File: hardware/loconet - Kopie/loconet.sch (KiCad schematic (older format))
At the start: 40 parts, among them J1 RJ12, J10 PWR, J11 PullUpEnable, J2 RJ12, J3 DCC, J4 Arduino Sockelleiste Pin01-15, J5 Arduino Sockelleiste Pin16-30, J6 PCA9685, J7 SCL/SDA, J8 I²C Connector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

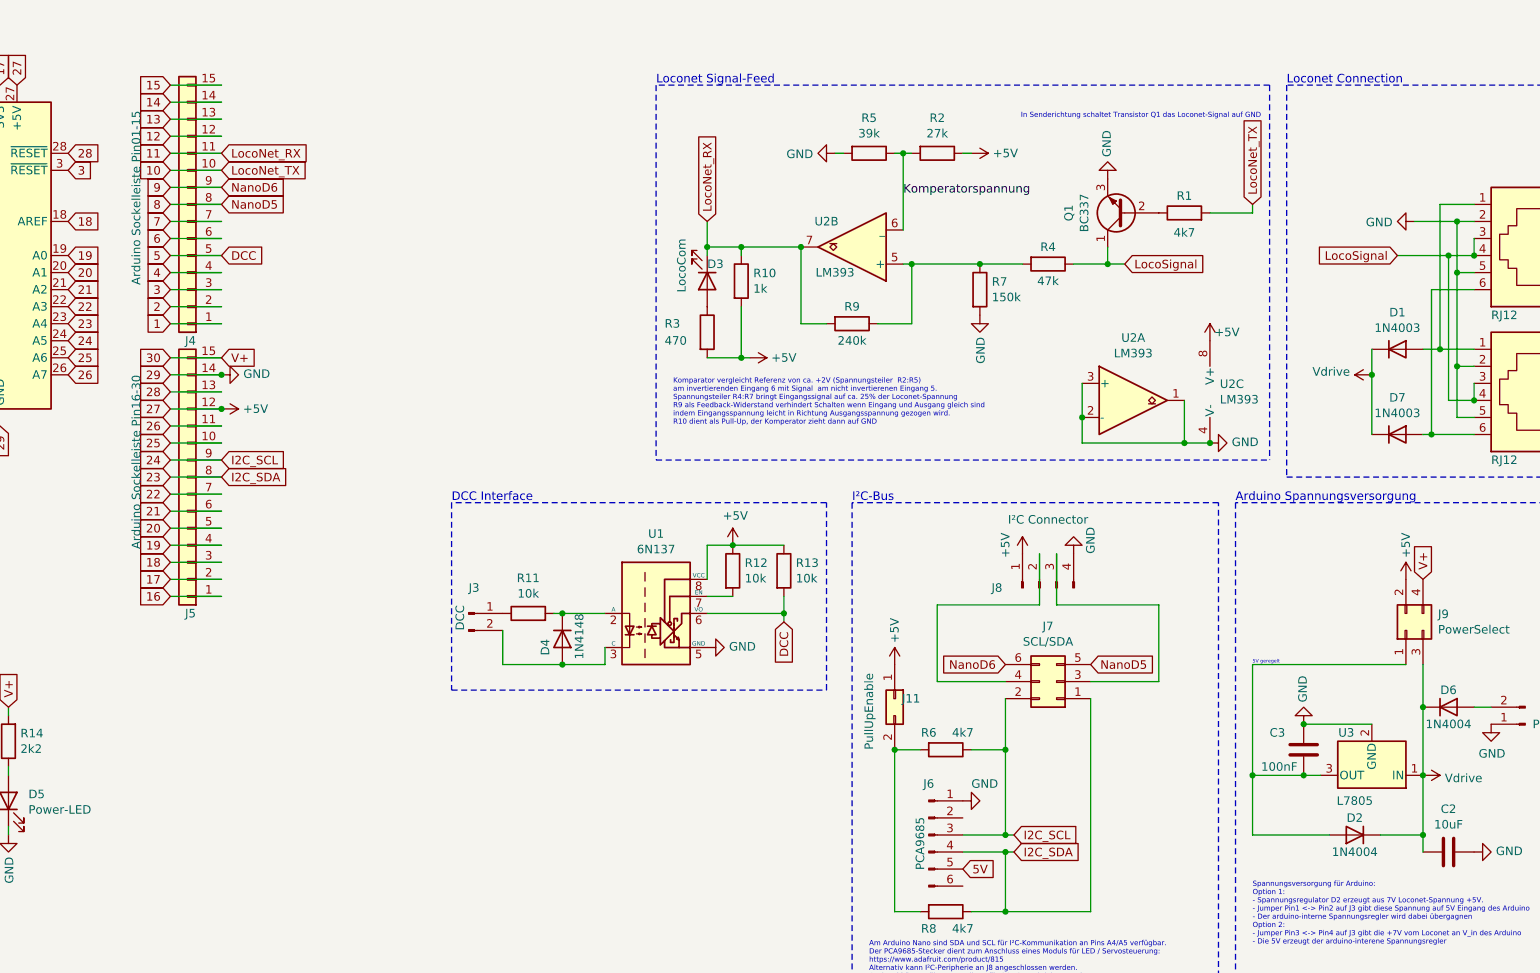
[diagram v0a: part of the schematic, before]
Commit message: Add variant hardware with loconet TX indicator LED
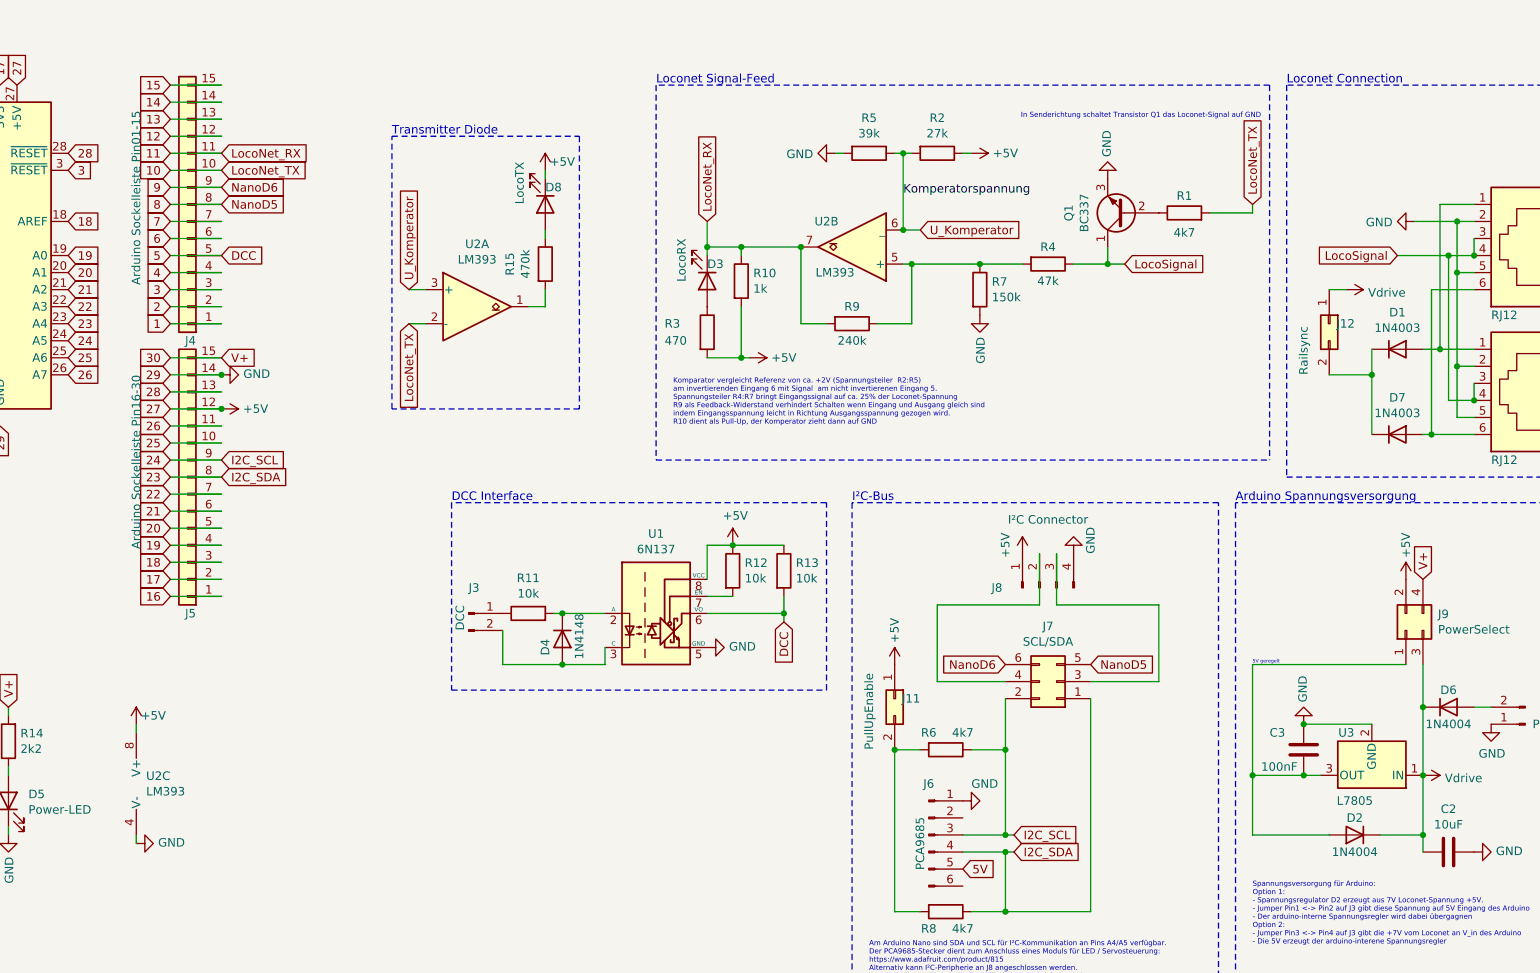
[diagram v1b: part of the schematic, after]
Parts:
- added D8: LocoTX, LED_THT:LED_D3.0mm, symbol Device:LED
- added J12: Railsync, Connector_PinHeader_2.54mm:PinHeader_2x01_P2.54mm_Vertical, symbol Connector_Generic:Conn_02x01
- added R15: 470k, Resistor_THT:R_Axial_DIN0207_L6.3mm_D2.5mm_P7.62mm_Horizontal, symbol Device:R
- D3: value LocoCom -> LocoRX
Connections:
- net +5V: now also D8.1 (K)
- net 10: now also U2.2 (-)
- net GND: no longer U2.1, U2.2 (-), U2.3 (+)
- net Vdrive: now also J12.1 (Pin_1); no longer D1.1 (K), D7.1 (K)
- net Komperatorspannung renamed U_Komperator
- net U_Komperator: now also U2.3 (+)
- new net: D1.1 (K), D7.1 (K), J12.2 (Pin_2)
- new net: R15.2, U2.1
- new net: D8.2 (A), R15.1
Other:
- note added: "Transmitter Diode"
- moved on the sheet: U2A, U2C
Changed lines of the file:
@@
 	1    0    0    -1
 $EndComp
-$Comp
-L Device:LED D3
-U 1 1 5EB93691
-P 5650 1850
-F 0 "D3" V 5550 1850 50  0000 L CNN
-F 1 "LocoCom" H 5400 1700 50  0000 L CNN
-F 2 "LED_THT:LED_D3.0mm" H 5650 1850 50  0001 C CNN
-F 3 "~" H 5650 1850 50  0001 C CNN
-	1    5650 1850
-	0    1    1    0
-$EndComp
 Wire Wire Line
 	10150 1400 9950 1400
@@
 	9900 1900 10150 1900
 Wire Wire Line
-	9550 2250 9550 2400
-Wire Wire Line
 	10150 1600 10150 1700
 Connection ~ 10150 1700
@@
 L Comparator:LM393 U2
 U 1 1 5EDB1EB7
-P 8150 2550
-F 0 "U2" H 8150 2917 50  0000 C CNN
-F 1 "LM393" H 8150 2826 50  0000 C CNN
-F 2 "" H 8150 2550 50  0001 C CNN
-F 3 "http://www.ti.com/lit/ds/symlink/lm393-n.pdf" H 8150 2550 50  0001 C CNN
-	1    8150 2550
+P 4300 2000
+F 0 "U2" H 4300 2367 50  0000 C CNN
+F 1 "LM393" H 4300 2276 50  0000 C CNN
+F 2 "" H 4300 2000 50  0001 C CNN
+F 3 "http://www.ti.com/lit/ds/symlink/lm393-n.pdf" H 4300 2000 50  0001 C CNN
+	1    4300 2000
 	1    0    0    -1
 $EndComp
@@
 L Comparator:LM393 U2
 U 3 1 5EDB30C8
-P 8700 2500
-F 0 "U2" H 8658 2546 50  0000 L CNN
-F 1 "LM393" H 8658 2455 50  0000 L CNN
-F 2 "" H 8700 2500 50  0001 C CNN
-F 3 "http://www.ti.com/lit/ds/symlink/lm393-n.pdf" H 8700 2500 50  0001 C CNN
-	3    8700 2500
+P 2400 4800
+F 0 "U2" H 2358 4846 50  0000 L CNN
+F 1 "LM393" H 2358 4755 50  0000 L CNN
+F 2 "" H 2400 4800 50  0001 C CNN
+F 3 "http://www.ti.com/lit/ds/symlink/lm393-n.pdf" H 2400 4800 50  0001 C CNN
+	3    2400 4800
 	1    0    0    -1
 $EndComp
@@
 L power:GND #PWR0101
 U 1 1 5EDB506B
-P 8600 2800
-F 0 "#PWR0101" H 8600 2550 50  0001 C CNN
-F 1 "GND" V 8605 2672 50  0000 R CNN
-F 2 "" H 8600 2800 50  0001 C CNN
-F 3 "" H 8600 2800 50  0001 C CNN
-	1    8600 2800
+P 2300 5150
+F 0 "#PWR0101" H 2300 4900 50  0001 C CNN
+F 1 "GND" V 2305 5022 50  0000 R CNN
+F 2 "" H 2300 5150 50  0001 C CNN
+F 3 "" H 2300 5150 50  0001 C CNN
+	1    2300 5150
 	0    -1   -1   0
 $EndComp
-Wire Wire Line
-	8600 2800 8450 2800
-Wire Wire Line
-	7850 2800 7850 2650
-Connection ~ 8600 2800
-Wire Wire Line
-	7850 2650 7850 2450
-Connection ~ 7850 2650
 $Comp
 L power:+5V #PWR0102
 U 1 1 5EDD0583
-P 8600 2200
-F 0 "#PWR0102" H 8600 2050 50  0001 C CNN
-F 1 "+5V" H 8700 2250 50  0000 C CNN
-F 2 "" H 8600 2200 50  0001 C CNN
-F 3 "" H 8600 2200 50  0001 C CNN
-	1    8600 2200
+P 2300 4450
+F 0 "#PWR0102" H 2300 4300 50  0001 C CNN
+F 1 "+5V" H 2400 4500 50  0000 C CNN
+F 2 "" H 2300 4450 50  0001 C CNN
+F 3 "" H 2300 4450 50  0001 C CNN
+	1    2300 4450
 	1    0    0    -1
 $EndComp
@@
 Entry Bus Bus
 	14700 -1150 14800 -1050
-Wire Wire Line
-	8450 2550 8450 2800
-Connection ~ 8450 2800
-Wire Wire Line
-	8450 2800 7850 2800
 $Comp
 L power:Vdrive #PWR07
 U 1 1 5F9BCDAB
-P 9550 2400
-F 0 "#PWR07" H 9350 2250 50  0001 C CNN
-F 1 "Vdrive" V 9568 2528 50  0000 L CNN
-F 2 "" H 9550 2400 50  0001 C CNN
-F 3 "" H 9550 2400 50  0001 C CNN
-	1    9550 2400
-	0    -1   -1   0
+P 9400 1900
+F 0 "#PWR07" H 9200 1750 50  0001 C CNN
+F 1 "Vdrive" V 9418 2028 50  0000 L CNN
+F 2 "" H 9400 1900 50  0001 C CNN
+F 3 "" H 9400 1900 50  0001 C CNN
+	1    9400 1900
+	0    1    1    0
 $EndComp
 $Comp
@@
 	0    1    1    0
 $EndComp
+Text Label 6800 1350 0    50   ~ 0
+Komperatorspannung
+Text GLabel 6900 1550 2    50   Input ~ 0
+U_Komperator
+Wire Wire Line
+	6800 1550 6900 1550
+Connection ~ 6800 1550
+$Comp
+L Device:R R15
+U 1 1 5FA24740
+P 4700 1750
+F 0 "R15" V 4493 1750 50  0000 C CNN
+F 1 "470k" V 4584 1750 50  0000 C CNN
+F 2 "Resistor_THT:R_Axial_DIN0207_L6.3mm_D2.5mm_P7.62mm_Horizontal" V 4630 1750 50  0001 C CNN
+F 3 "~" H 4700 1750 50  0001 C CNN
+	1    4700 1750
+	1    0    0    -1
+$EndComp
+Wire Wire Line
+	2300 4450 2300 4500
+Wire Wire Line
+	2300 5100 2300 5150
+$Comp
+L Device:LED D8
+U 1 1 5FA41AAA
+P 4700 1400
+F 0 "D8" V 4600 1400 50  0000 L CNN
+F 1 "LocoTX" H 4450 1250 50  0000 L CNN
+F 2 "LED_THT:LED_D3.0mm" H 4700 1400 50  0001 C CNN
+F 3 "~" H 4700 1400 50  0001 C CNN
+	1    4700 1400
+	0    1    1    0
+$EndComp
+Wire Wire Line
+	4700 1550 4700 1600
+Wire Wire Line
+	4700 1900 4700 2000
+Wire Wire Line
+	4700 1250 4700 1200
+Text GLabel 3900 1900 1    50   Input ~ 0
+U_Komperator
+Wire Wire Line
+	3900 1900 4000 1900
+Text GLabel 3900 2100 3    50   Input ~ 0
+LocoNet_TX
+Wire Wire Line
+	3900 2100 4000 2100
+Wire Wire Line
+	4600 2000 4700 2000
+$Comp
+L power:+5V #PWR0107
+U 1 1 5FA7987F
+P 4700 1200
+F 0 "#PWR0107" H 4700 1050 50  0001 C CNN
+F 1 "+5V" H 4800 1250 50  0000 C CNN
+F 2 "" H 4700 1200 50  0001 C CNN
+F 3 "" H 4700 1200 50  0001 C CNN
+	1    4700 1200
+	1    0    0    -1
+$EndComp
+Wire Notes Line
+	3800 1000 4900 1000
+Wire Notes Line
+	4900 1000 4900 2600
+Wire Notes Line
+	4900 2600 3800 2600
+Wire Notes Line
+	3800 2600 3800 1000
+Text Notes 3800 1000 0    50   ~ 0
+Transmitter Diode
+$Comp
+L Device:LED D3
+U 1 1 5EB93691
+P 5650 1850
+F 0 "D3" V 5550 1850 50  0000 L CNN
+F 1 "LocoRX" H 5400 1700 50  0000 L CNN
+F 2 "LED_THT:LED_D3.0mm" H 5650 1850 50  0001 C CNN
+F 3 "~" H 5650 1850 50  0001 C CNN
+	1    5650 1850
+	0    1    1    0
+$EndComp
+$Comp
+L Connector_Generic:Conn_02x01 J12
+U 1 1 5FB03C5E
+P 9300 2100
+F 0 "J12" V 9300 2250 50  0000 R CNN
+F 1 "Railsync" H 9600 1950 50  0000 R CNN
+F 2 "Connector_PinHeader_2.54mm:PinHeader_2x01_P2.54mm_Vertical" H 9300 2100 50  0001 C CNN
+F 3 "~" H 9300 2100 50  0001 C CNN
+	1    9300 2100
+	0    1    1    0
+$EndComp
+Wire Wire Line
+	9300 1900 9400 1900
+Wire Wire Line
+	9550 2250 9550 2400
+Wire Wire Line
+	9300 2400 9550 2400
 Connection ~ 9550 2400
 Wire Wire Line
 	9550 2400 9550 2750
-Text Label 6800 1350 0    50   ~ 0
-Komperatorspannung
 $EndSCHEMATC

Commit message: Einige Verbesserungen am PCB Layout
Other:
- moved on the sheet: C2, C3, D2, D4, D6, J10, J11, J3, J6, J7, J8, J9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

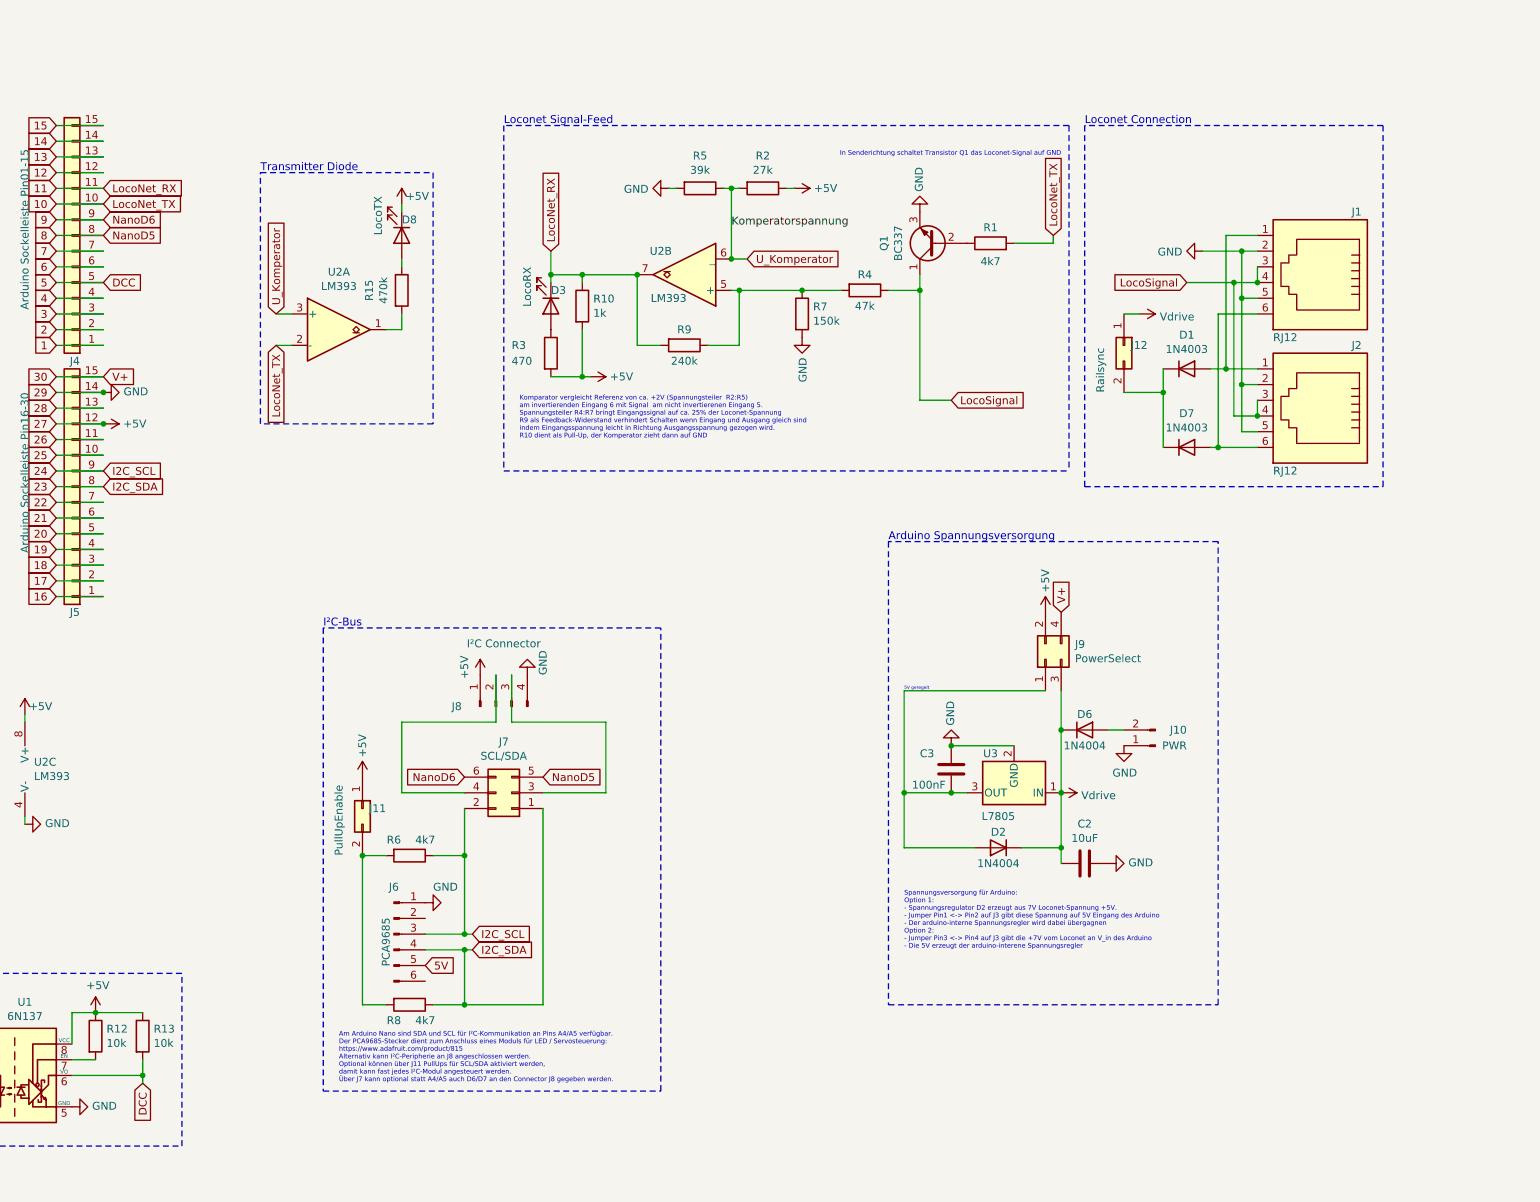
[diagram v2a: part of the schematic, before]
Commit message: Added some capacitors
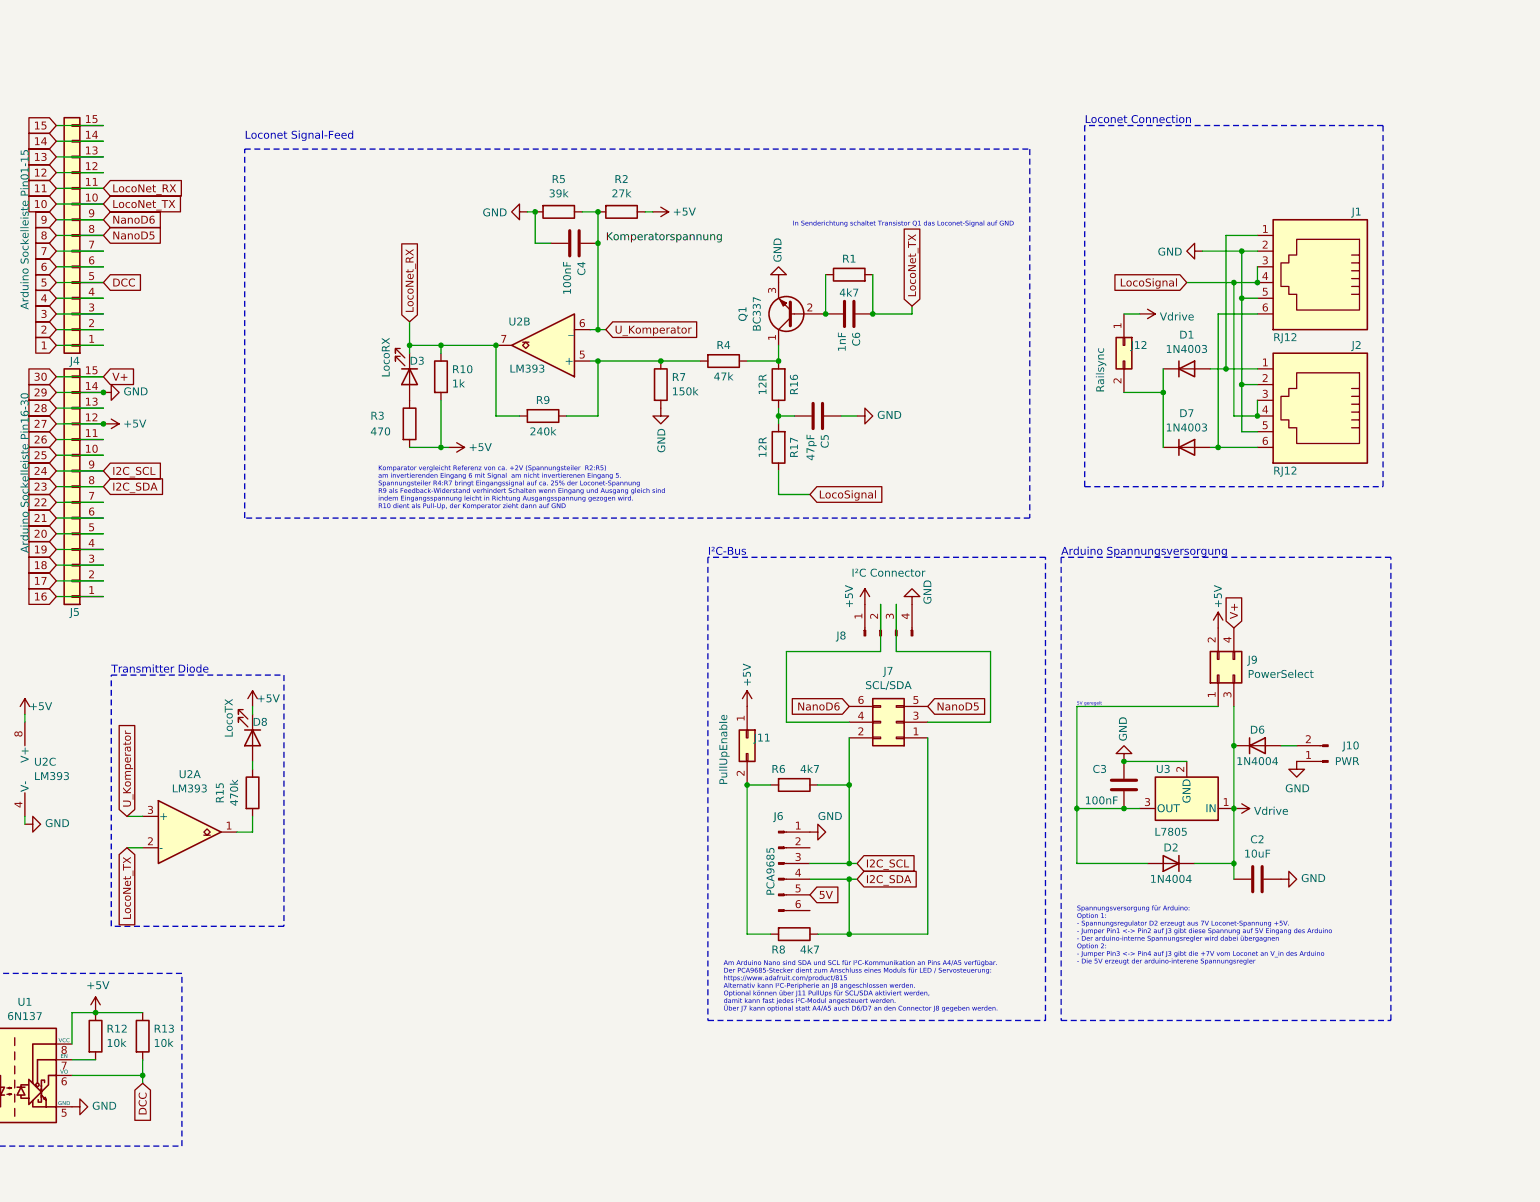
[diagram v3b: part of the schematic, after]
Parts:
- added C4: 100nF, Capacitor_THT:C_Disc_D4.3mm_W1.9mm_P5.00mm, symbol Device:C
- added C5: 47pF, Capacitor_THT:C_Disc_D4.3mm_W1.9mm_P5.00mm, symbol Device:C
- added C6: 1nF, Capacitor_THT:C_Disc_D4.3mm_W1.9mm_P5.00mm, symbol Device:C
- added R16, R17: 12R, Resistor_THT:R_Axial_DIN0207_L6.3mm_D2.5mm_P7.62mm_Horizontal, symbol Device:R
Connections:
- net 10: now also C6.1
- net GND: now also C4.2, C5.1
- net LocoSignal: now also R17.1; no longer Q1.1 (C), R4.1
- net U_Komperator: now also C4.1
- net at Q1.2 (B), R1.1: now also C6.2
- new net: Q1.1 (C), R16.2, R4.1
- new net: C5.2, R16.1, R17.2
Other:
- moved on the sheet: C2, C3, D2, D3, D6, D8, J10, J11, J6, J7, J8, J9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
